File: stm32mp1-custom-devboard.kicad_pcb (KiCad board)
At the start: 4 copper layers, 120 x 72 mm, 80 parts, among them Con1 52746-0671, Con2 505110-2491, Con3 2041119-1, Con4 USB_C_Wurth_632723130112, P1 Main Power Supply, Q1 BC847B, U1 TPS61169DCKR, U2 MCP1703T-3302E, U3 ST1S10PHR, U4 ST1S09IPUR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

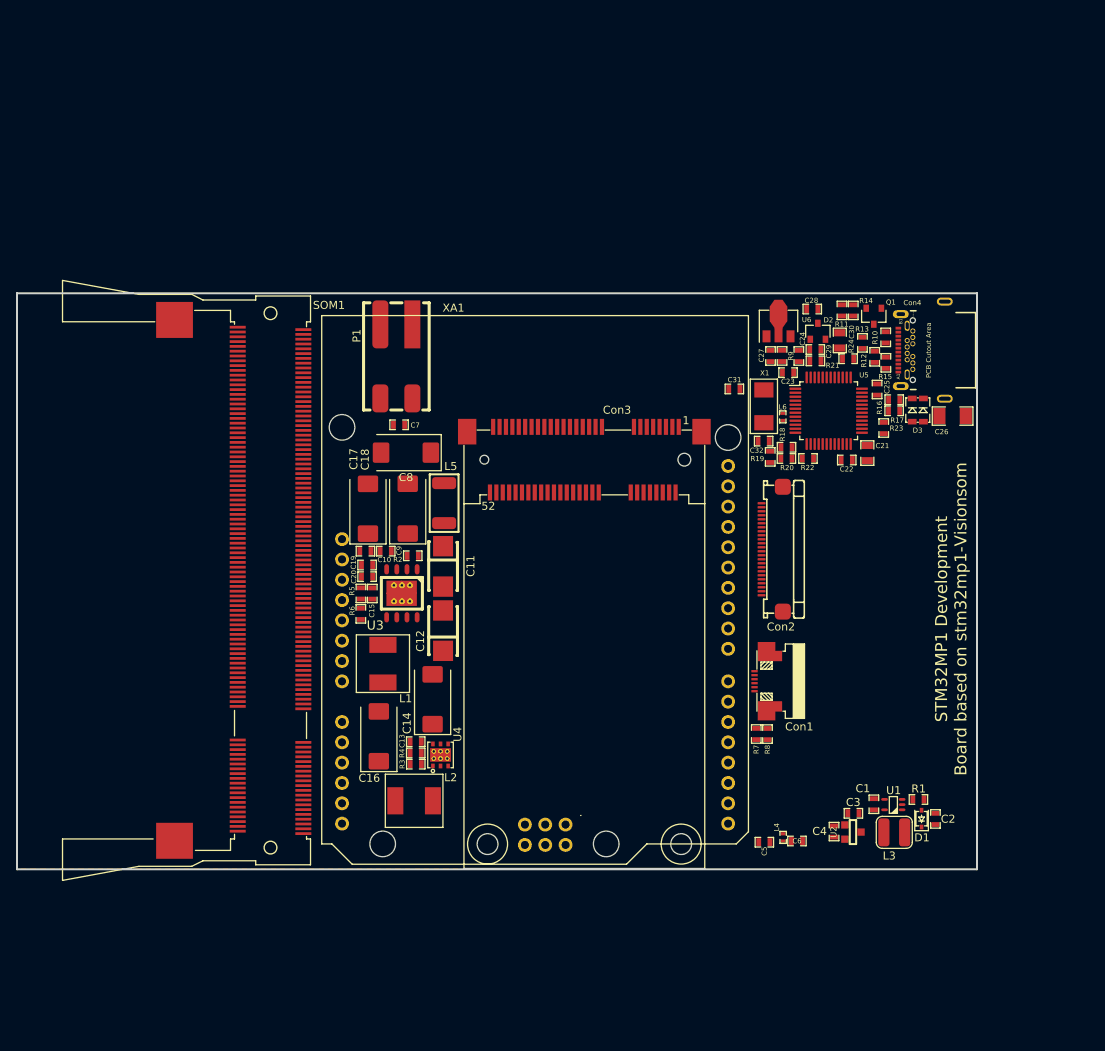
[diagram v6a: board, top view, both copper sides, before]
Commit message: Added ethernet and usb module
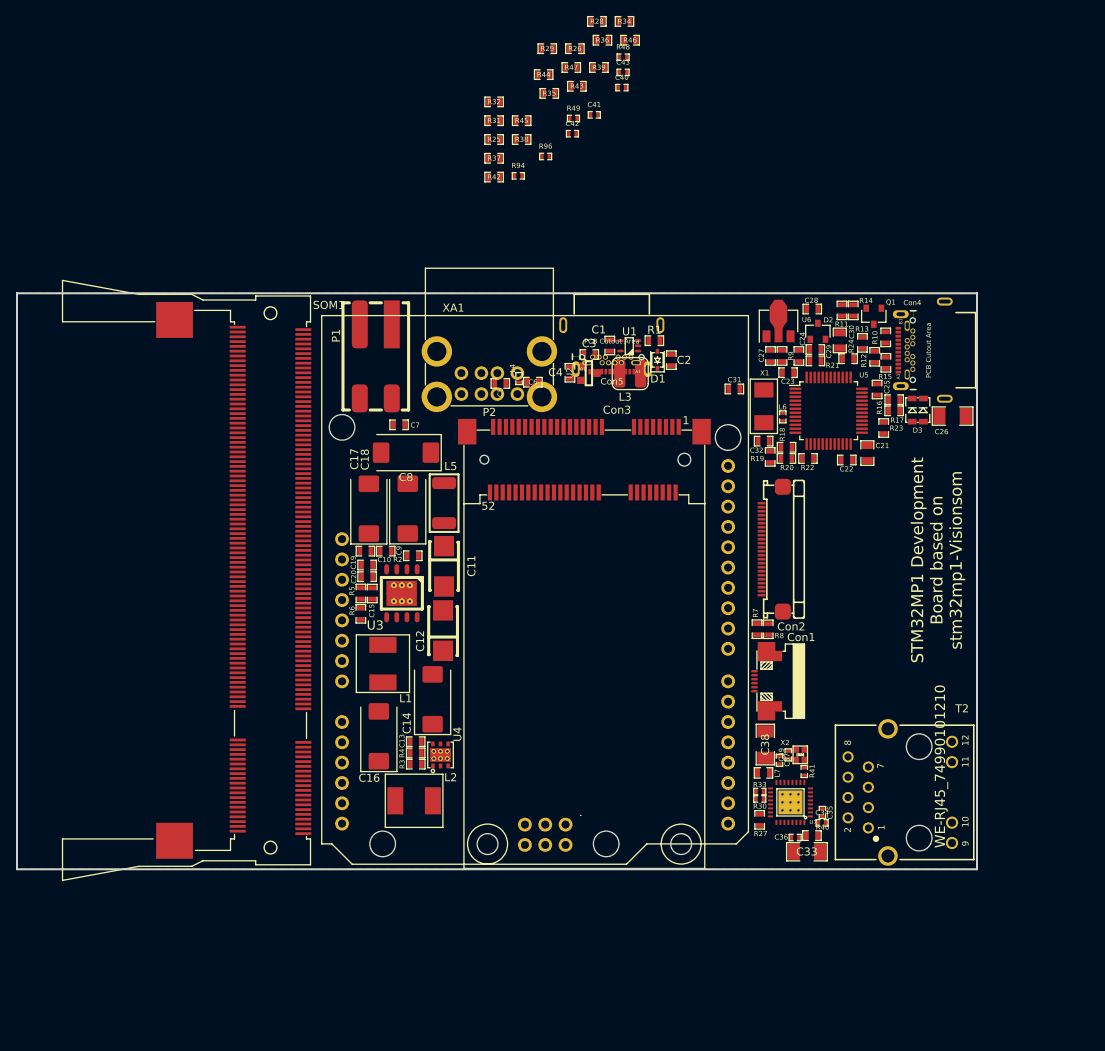
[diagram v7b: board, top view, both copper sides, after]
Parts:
- added C33: 22uF6V3, Smd_Tantal:22uF6V3_1206, F.Cu at (191.8, 136.2)
- added C34: 100nF/50V, Capacitors_Smd_0402:100nF_0402, F.Cu at (193.8, 132.6)
- added C35: 100nF/50V, Capacitors_Smd_0402:100nF_0402, F.Cu at (193.8, 131.3)
- added C36: 100nF/50V, Capacitors_Smd_0402:100nF_0402, F.Cu at (190.4, 134.4)
- added C37: 100nF/50V, Capacitors_Smd_0402:100nF_0402, F.Cu at (188.4, 124.8)
- added C38: 22uF6V3, Smd_Tantal:22uF6V3_1206, F.Cu at (186.7, 122.8)
- added C39: 1uF/10V, Capacitors_Smd_0402:1uF_0402, F.Cu at (189.5, 124.1)
- added C40: 100nF/50V, Capacitors_Smd_0402:100nF_0402, F.Cu at (168.7, 40.7)
- added C41: 100nF/50V, Capacitors_Smd_0402:100nF_0402, F.Cu at (165.3, 44.1)
- added C42: 100nF/50V, Capacitors_Smd_0402:100nF_0402, F.Cu at (162.5, 46.5)
- added C43: 100nF/50V, Capacitors_Smd_0402:100nF_0402, F.Cu at (168.9, 38.8)
- added Con5: USB_C_Wurth_632723130112, Connector_USB:USB_C_632723130112, F.Cu at (167.5, 71.6)
- added L7: BLM18PG121SN1D, Inductors:BLM18PG121SN1D_SM0603, F.Cu at (186.4, 126.4)
- added P2: USB-A-D-RA, Connector_USB:USB-A-D-RA, F.Cu at (152.2, 73.7)
- added R25: 1k, Resistor_Smd_0603:1k_0603, F.Cu at (152.7, 47.2)
- added R26: 1k, Resistor_Smd_0603:1k_0603, F.Cu at (162.8, 35.8)
- added R27: 1k, Resistor_Smd_0603:1k_0603, F.Cu at (185.9, 132.2)
- added R28: 1k, Resistor_Smd_0603:1k_0603, F.Cu at (165.6, 32.4)
- added R29: 1k, Resistor_Smd_0603:1k_0603, F.Cu at (159.4, 35.8)
- added R30: 33R, Resistor_Smd_0402:33R_0402, F.Cu at (186.0, 129.6)
- added R31: 1k, Resistor_Smd_0603:1k_0603, F.Cu at (152.7, 44.8)
- added R32: 1k, Resistor_Smd_0603:1k_0603, F.Cu at (152.7, 42.5)
- added R33: 33R, Resistor_Smd_0402:33R_0402, F.Cu at (186.0, 128.7)
- added R34: 1k, Resistor_Smd_0603:1k_0603, F.Cu at (169.0, 32.4)
- added R35: 1k, Resistor_Smd_0603:1k_0603, F.Cu at (159.6, 41.4)
- added R36: 6k49, Resistor_Smd_0603:6k49_0603, F.Cu at (166.3, 34.8)
- added R37: 1k, Resistor_Smd_0603:1k_0603, F.Cu at (152.7, 49.5)
- added R38: 4k7_NM, Resistor_Smd_0603:4k7_0603, F.Cu at (156.2, 47.2)
- added R39: 1k, Resistor_Smd_0603:1k_0603, F.Cu at (165.8, 38.2)
- added R40: 10k, Resistor_Smd_0603:10k_0603, F.Cu at (192.5, 134.2)
- added R41: 33R, Resistor_Smd_0402:33R_0402, F.Cu at (191.5, 126.2)
- added R42: 4k7, Resistor_Smd_0603:4k7_0603, F.Cu at (152.7, 51.9)
- added R43: 4k7, Resistor_Smd_0603:4k7_0603, F.Cu at (163.1, 40.5)
- added R44: 1k_NM, Resistor_Smd_0603:1k_0603, F.Cu at (158.9, 39.1)
- added R45: 1k_NM, Resistor_Smd_0603:1k_0603, F.Cu at (156.2, 44.8)
- added R46: 220R, Resistor_Smd_0603:220R_0603, F.Cu at (169.7, 34.8)
- added R47: 220R, Resistor_Smd_0603:220R_0603, F.Cu at (162.4, 38.2)
- added R48: 49R9_1%, Resistor_Smd_0402:49R9_0402, F.Cu at (168.9, 36.9)
- added R49: 49R9_1%, Resistor_Smd_0402:49R9_0402, F.Cu at (162.7, 44.6)
- added R94: 49R9_1%, Resistor_Smd_0402:49R9_0402, F.Cu at (155.8, 51.7)
- added R96: 49R9_1%, Resistor_Smd_0402:49R9_0402, F.Cu at (159.2, 49.3)
- added T2: WE-RJ45_74990101210, RJ45_Ethernet_Transformer:WE-RJ45_74990101210, F.Cu at (205.9, 128.8)
- added U7: KSZ8041NL_RNL, Communication_Interfaces:KSZ8041NL_RNL_QFN32, F.Cu at (189.8, 130.1)
- added X2: ECS-2016MV-250-CN-TR, Resonators:520-2016MV-250-CNT, F.Cu at (191.0, 124.1)
- moved C4 66.2 mm to (162.2, 76.3)
- moved D1 66.2 mm to (173.2, 74.7)
- moved L3 66.2 mm to (169.8, 76.4)
- moved U1 66.2 mm to (169.6, 73.0)
- moved C1 66.2 mm to (167.2, 72.9)
- moved C2 66.2 mm to (174.9, 74.8)
- moved C3 66.2 mm to (164.7, 74.1)
- moved C5 66.2 mm to (153.5, 77.7)
- moved C6 66.2 mm to (157.6, 77.5)
- moved L4 66.2 mm to (155.9, 77.1)
- moved R1 66.2 mm to (172.8, 72.3)
- moved U2 66.2 mm to (164.6, 76.4)
- moved R8 13.1 mm to (187.0, 108.4)
- moved R7 13.1 mm to (185.6, 108.4)
- moved P1 2.57 mm to (138.0, 74.3)
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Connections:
- D2 pad 1: (no net) -> 5V
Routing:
- added copper zone on In1.Cu, net 3V3
- removed copper zone on In1.Cu, net VDD

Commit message: Added new USB connectors on schematic, figurated elements on pcb
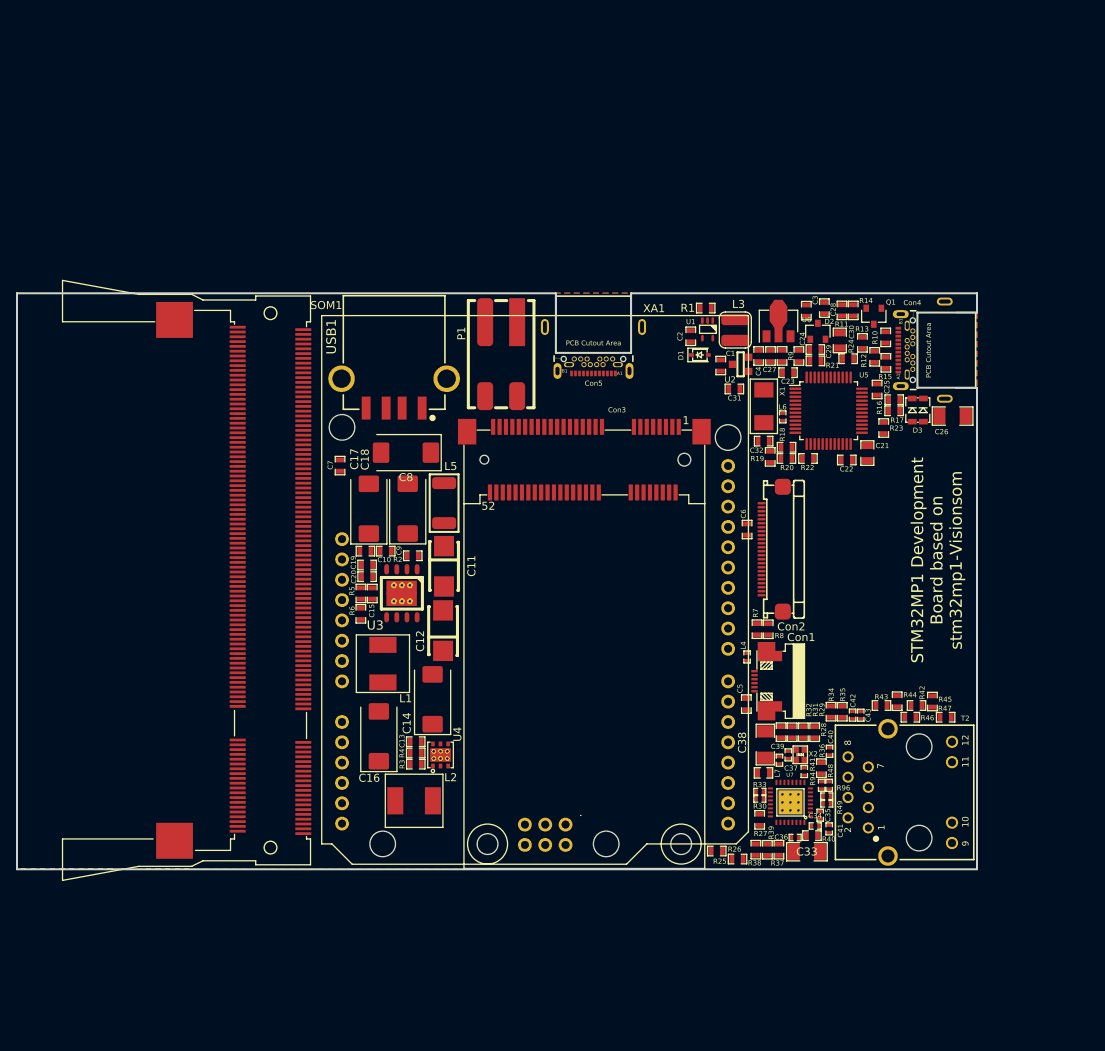
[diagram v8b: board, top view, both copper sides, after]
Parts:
- removed P2: USB-A-D-RA, Connector_USB:USB-A-D-RA
- added USB1: USB-A-Wurth-62900416021, Connector_USB:Wurth-62900416021, F.Cu at (140.2, 73.8)
- moved R26 101.9 mm to (180.6, 136.1)
- moved R39 100.0 mm to (186.9, 136.0), turned to 270 degrees
- moved R36 95.0 mm to (193.7, 125.8), turned to 270 degrees
- moved R25 95.0 mm to (183.2, 137.1)
- moved R48 94.6 mm to (194.6, 127.9), turned to 90 degrees
- moved C41 94.0 mm to (194.6, 133.4), turned to 270 degrees
- moved R47 93.7 mm to (209.2, 119.4), turned to 180 degrees
- moved R38 93.5 mm to (185.5, 136.0), turned to 90 degrees
- moved R37 93.5 mm to (188.3, 136.0), turned to 270 degrees
- moved R28 92.9 mm to (192.8, 121.3), turned to 270 degrees
- moved R46 91.6 mm to (204.8, 119.4), turned to 180 degrees
- moved R49 91.3 mm to (194.3, 130.2)
- moved R29 91.2 mm to (191.4, 121.3), turned to 270 degrees
- moved R34 90.1 mm to (194.9, 118.7), turned to 90 degrees
- moved R44 89.9 mm to (203.1, 117.4), turned to 270 degrees
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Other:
- outline, holes or cut-outs redrawn
